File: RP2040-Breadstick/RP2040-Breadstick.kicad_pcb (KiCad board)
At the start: 6 copper layers, 10.2 x 163.8 mm, 94 parts, among them IC501 LM66200DRLR, J111 Conn_01x01, J112 Conn_01x01, J113 Conn_01x01, J114 Conn_01x01, J115 Conn_01x01, J116 Conn_01x01, J117 Conn_01x01, J118 Conn_01x01, J119 Conn_01x01, J120 Conn_01x02, J121 Conn_01x01, J122 Conn_01x01, J123 Conn_01x01, J124 Conn_01x01, J125 Conn_01x01, J126 Conn_01x01, J127 Conn_01x01, J128 Conn_01x01, J129 Conn_01x01, J130 Conn_01x02, J501 Conn_01x05, J502 Conn_01x05, J601 USB_C_Receptacle_USB2.0, Q301 SSM3K56FS,LF, Q302 SSM3K56FS,LF, U201 RP2040, U202 16MB Flash, U401 6-Axis IMU, U501 AP2112K-3.3TRG1, Y201 12MHz

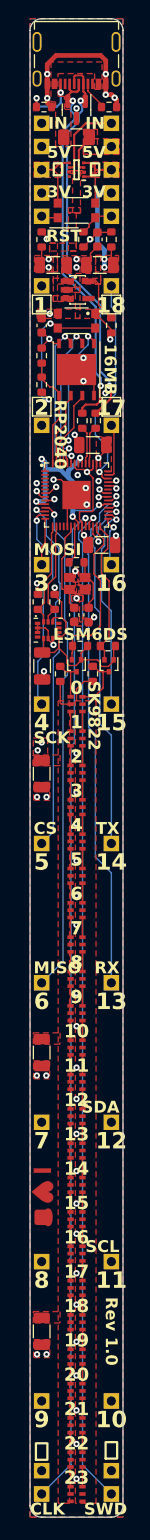
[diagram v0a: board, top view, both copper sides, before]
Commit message: removed parts not needed for LEDs and IMU
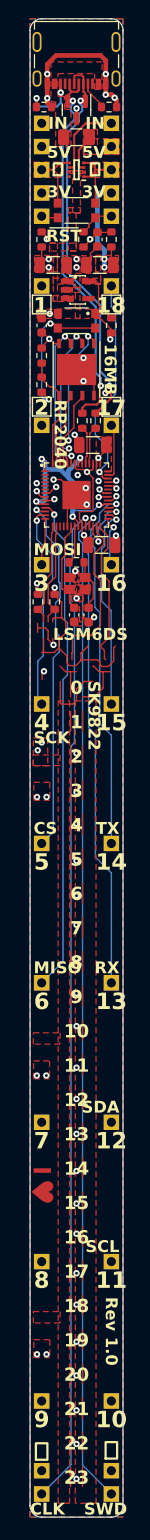
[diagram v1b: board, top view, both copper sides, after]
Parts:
- removed ?: , clipboard:a90286b4-b738-4e00-aca9-2c8c50e98d30
- removed C302, C304, C306, C402: 10uF 1206 6V3, Capacitor_SMD:C_1206_3216Metric
- removed LED301, LED302, LED303, LED304, LED305, LED306, LED307, LED308, LED309, LED310, LED311, LED312, LED313, LED314, LED315, LED316, LED317, LED318, LED319, LED320, LED321, LED322, LED323, LED324: SK9822, _Breadstick_Footprints:SK9822-2020
- removed Q301, Q302: SSM3K56FS,LF, Package_TO_SOT_SMD:SOT-416
- removed R301, R302, R303, R304: 10k 0603, Resistor_SMD:R_0603_1608Metric
- removed U401: 6-Axis IMU, LSM6DSMTR:PQFN50P300X250X86-14N
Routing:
- net (no net): track 0.00 -> 110.5 mm
- net /Addressable RGB LEDs/DATA: track 6.58 -> 0.00 mm
- net /Addressable RGB LEDs/CLK: track 4.77 -> 0.00 mm
- net Net-(LED321-DATA_OUT): track 2.17 -> 0.00 mm
- net Net-(LED306-DATA_OUT): track 2.15 -> 0.00 mm
- net Net-(LED306-CLK_OUT): track 2.15 -> 0.00 mm
- net Net-(LED304-DATA_OUT): track 2.15 -> 0.00 mm
- net Net-(LED304-CLK_OUT): track 2.15 -> 0.00 mm
- net Net-(LED323-DATA_OUT): track 2.15 -> 0.00 mm
- net Net-(LED323-CLK_OUT): track 2.15 -> 0.00 mm
- net Net-(LED320-DATA_OUT): track 2.15 -> 0.00 mm
- net Net-(LED320-CLK_OUT): track 2.15 -> 0.00 mm
- net Net-(LED319-DATA_OUT): track 2.15 -> 0.00 mm
- net Net-(LED319-CLK_OUT): track 2.15 -> 0.00 mm
- net Net-(LED318-DATA_OUT): track 2.15 -> 0.00 mm
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
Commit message: cleaned up unused tracks/vias
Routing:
- net (no net): track 110.5 -> 0.00 mm
- net /Power/VHI: track 65.4 -> 2.82 mm, vias 4 -> 2
- net /3V3: track 81.3 -> 57.7 mm
- net /RP2040/LED_CLK: track 18.0 -> 0.00 mm
- net /RP2040/LED_DATA: track 16.2 -> 0.00 mm
- net GND: track 77.9 -> 72.2 mm, vias 55 -> 25
- net /RP2040/I2C0-SCL: track 11.4 -> 9.73 mm
- net /RP2040/I2C0-SDA: track 11.4 -> 9.74 mm
- removed copper zone on In2.Cu, net /Power/VHI
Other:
- board text removed: "0"
- board text removed: "19"
- board text removed: "20"
- board text removed: "21"
- board text removed: "22"
- board text removed: "23"
- board text removed: "RP2040 SK9822 LSM6DS"
